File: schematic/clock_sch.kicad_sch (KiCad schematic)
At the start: 19 parts, among them SW1 SW_Push, SW2 SW_SPDT, U1 LM555, U2 LM555, U3 LM555, U4 74LS04, U5 74LS08, U6 74LS32

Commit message: missing R1
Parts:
- added R1: 1K, symbol Device:R
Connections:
- net VCC: now also R6.1, R1.1; no longer R2.1, U1.7 (DIS)
- new net: R1.2, R2.1, U1.7 (DIS)
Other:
- moved on the sheet: C5, C6, R2, RV1, U1

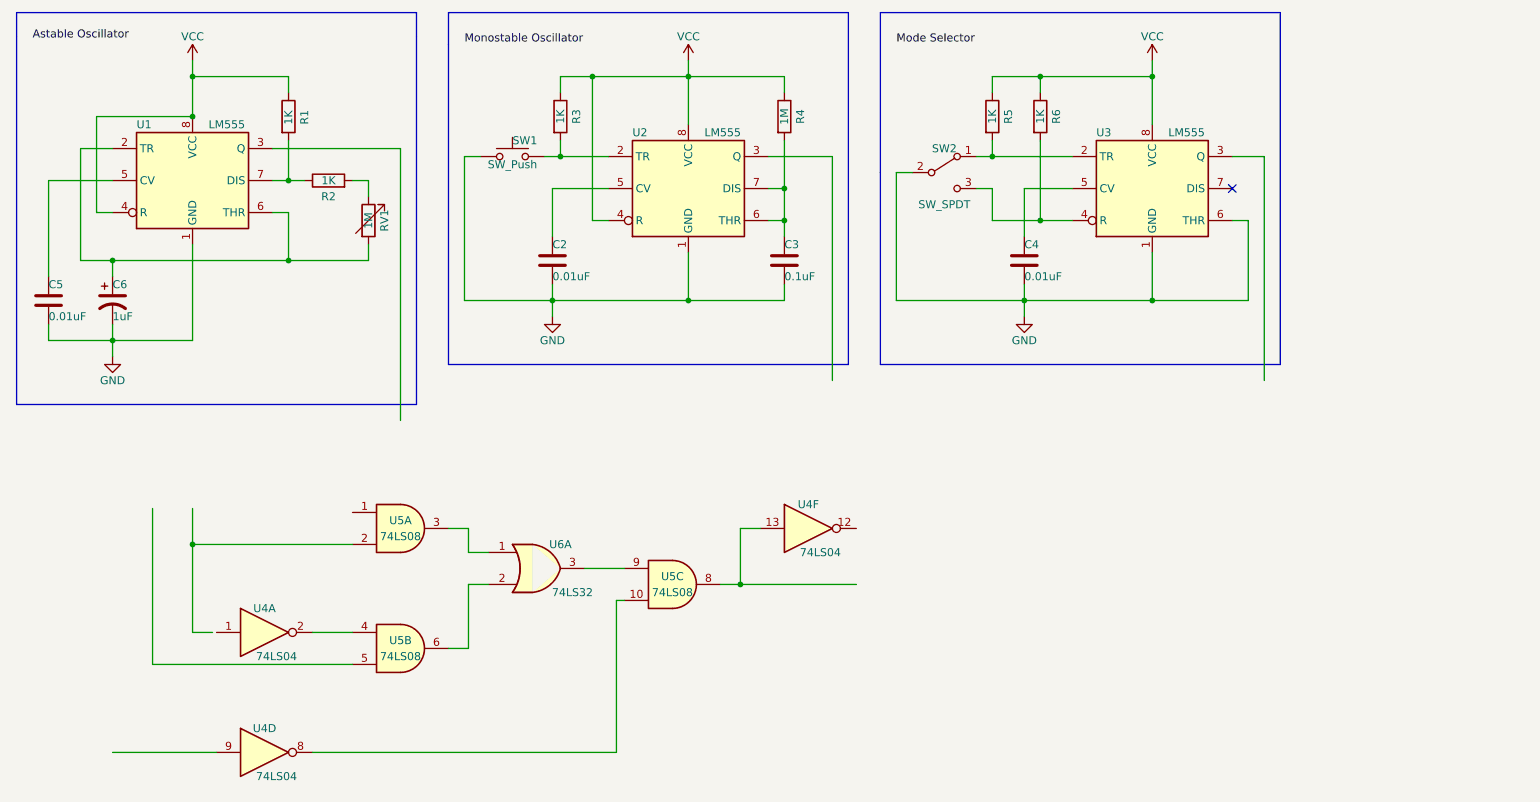
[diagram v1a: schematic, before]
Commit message: connected timers to logic circuit
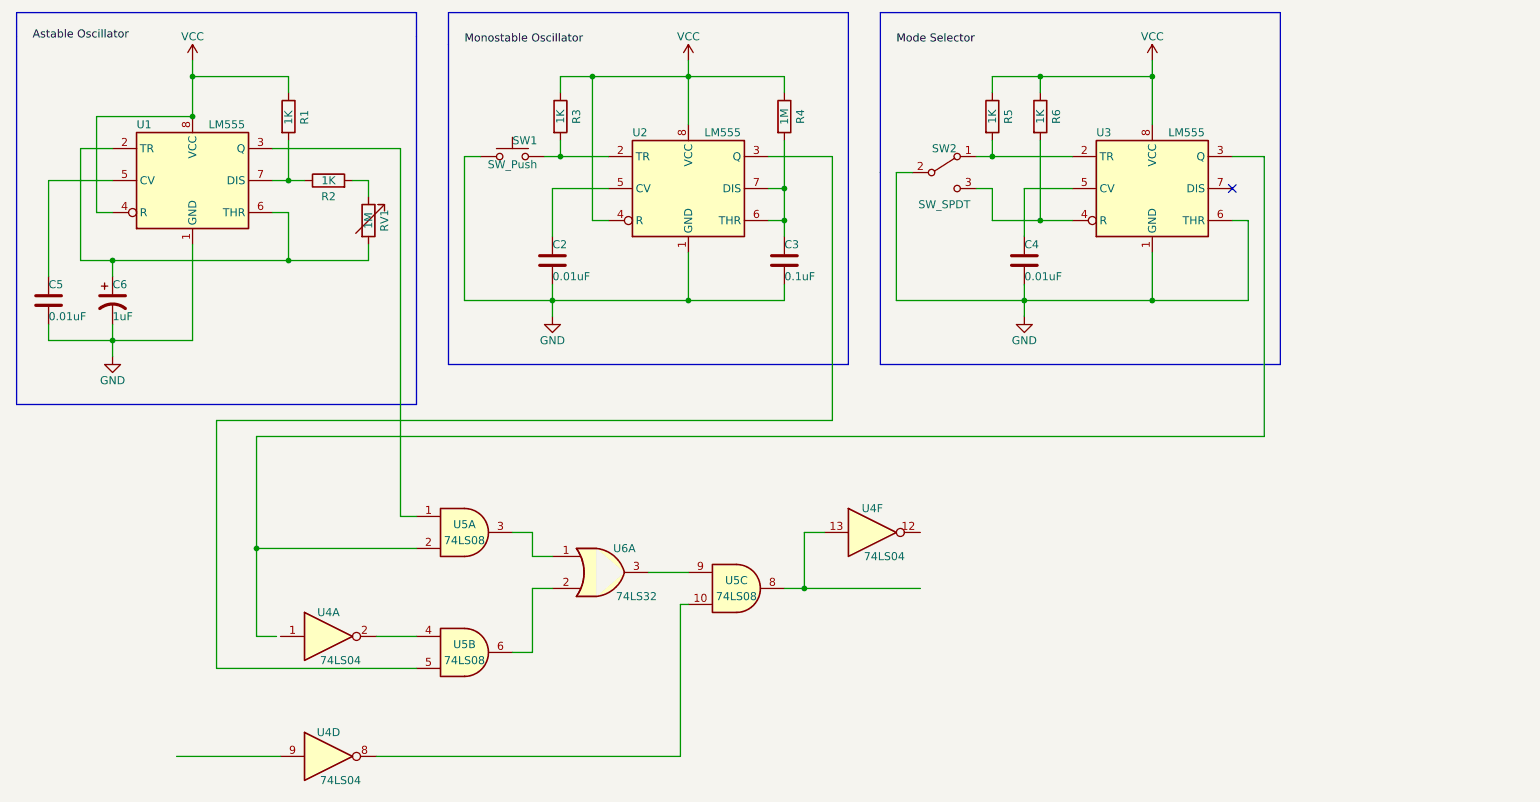
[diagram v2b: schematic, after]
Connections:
- net at U1.3 (Q): now also U5.1
- net at U5.5: now also U2.3 (Q)
- net at U5.2: now also U3.3 (Q)
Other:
- moved on the sheet: U4A, U4D, U4F, U5A, U5B, U5C, U6A

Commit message: added global labels
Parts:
- added D1, D2, D3: LED, symbol Device:LED
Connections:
- net VCC is gone; now on net GND: R1.1, R3.1, R4.1, R5.1, R6.1, U1.4 (R), U1.8 (VCC), U2.4 (R), U2.8 (VCC), U3.8 (VCC)
- net GND: now also D1.1 (K), D2.1 (K), D3.1 (K)
- net N_CLK: now reaches U4.12
- net CLK: now reaches U4.13, U5.8
- net at U1.3 (Q), U5.1: now also D1.2 (A)
- net at U4.1: now also U3.3 (Q), U5.2, D3.2 (A)
- net at U2.3 (Q), U5.5: now also D2.2 (A)
- net HLT: now reaches U4.9
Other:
- note added: "Astable Oscillator"
- note added: "Mode Selector"
- note added: "Monostable Oscillator"
- moved on the sheet: C4, C5, C6, R1, R2, R5, R6, RV1, SW2, U1, U3
